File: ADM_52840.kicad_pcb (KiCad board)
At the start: 2 copper layers, 45 x 60 mm, 7 parts, among them U1 HolyIOT_NRF52840

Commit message: route & 3D
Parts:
- added C1: 100nF, LEGACY:SM0603, F.Cu at (118.6, 108.6)
- added C3: 1nF, LEGACY:SM0603, F.Cu at (103.7, 94.0)
- added C4: 10microF, LEGACY:SM0805, F.Cu at (131.9, 121.8)
- added C5: 10microF, LEGACY:SM0805, F.Cu at (115.6, 127.2)
- added C6: 10microF, LEGACY:SM0805, F.Cu at (116.7, 123.5)
- added D1: LED1, LEGACY:SM0603, F.Cu at (104.9, 99.0)
- added D2: LED2, LEGACY:SM0603, F.Cu at (107.8, 99.0)
- added D3: LED3, LEGACY:SM0603, F.Cu at (118.4, 118.5)
- added D4: MBR120, LEGACY:SOD-123, F.Cu at (125.4, 132.7)
- added D5: SK6812, LEGACY:WS2812B, F.Cu at (106.6, 111.8)
- added P1: USB_micro_B, LEGACY:USB_Micro-B, F.Cu at (132.0, 138.9)
- added Q1: DMP2045U, LEGACY:SOT23, F.Cu at (123.7, 129.3)
- added R1: 806K, LEGACY:SM0603, F.Cu at (106.3, 95.3)
- added R2: 2M, LEGACY:SM0603, F.Cu at (106.3, 92.2)
- added R3: 10K, LEGACY:SM0603, F.Cu at (131.9, 119.4)
- added R4: 1K, LEGACY:SM0603, F.Cu at (115.8, 119.0)
- added R5: 100K, LEGACY:SM0603, F.Cu at (119.1, 127.3)
- added R6: 100K, LEGACY:SM0603, F.Cu at (125.4, 137.7)
- added R7: 330, LEGACY:SM0603, F.Cu at (104.9, 102.3)
- added R8: 330, LEGACY:SM0603, F.Cu at (107.8, 102.3)
- added SW1: BTN1, LEGACY:SWITCH_CMS, F.Cu at (107.7, 123.7)
- added SW2: BTN2, LEGACY:SWITCH_CMS, F.Cu at (107.7, 130.9)
- added SW3: RESET, LEGACY:SWITCH_CMS, F.Cu at (107.7, 138.1)
- added U2: GD25Q16, LEGACY:SON80P400X300X60-10N, F.Cu at (121.0, 104.4)
- added U3: MCP73831, Package_TO_SOT_SMD:SOT-23-5, F.Cu at (123.4, 120.3)
- added U4: AP2127K-3.3, LEGACY:SOT23-5, F.Cu at (123.4, 124.9)
- C2: value C -> 10microF; footprint MWL:SM0805 -> LEGACY:SM0805
- J1: value (none) -> JST; footprint Connector_PinHeader_2.54mm:PinHeader_1x22_P2.54mm_Vertical -> Connector_JST:JST_PH_S2B-PH-SM4-TB_1x02-1MP_P2.00mm_Horizontal
- J2: value (none) -> SK6812_OUT; footprint Connector_PinHeader_2.54mm:PinHeader_1x18_P2.54mm_Vertical -> LEGACY:pin_array_3x1
- J3: value (none) -> Conn_01x15_Male; footprint Connector_PinHeader_2.54mm:PinHeader_1x10_P2.54mm_Vertical -> Connector_PinSocket_2.54mm:PinSocket_1x15_P2.54mm_Vertical
- J4: value (none) -> Conn_01x19_Male; footprint Connector_PinHeader_1.27mm:PinHeader_2x05_P1.27mm_Vertical_SMD -> Connector_PinSocket_2.54mm:PinSocket_1x18_P2.54mm_Vertical
- J5: value (none) -> JTAG; footprint Connector_PinHeader_2.54mm:PinHeader_1x06_P2.54mm_Vertical -> Connector_PinSocket_2.54mm:PinSocket_2x03_P2.54mm_Vertical
- U1: footprint MWL:HolyIOT-NRF52840-Module -> LEGACY:HolyIOT-NRF52840-Module
- moved J1 57.7 mm to (135.2, 128.5), turned to 90 degrees
- moved J4 56.4 mm to (98.3, 84.2)
- moved J2 41.5 mm to (98.3, 135.3), turned to 270 degrees
- moved J3 39.8 mm to (138.7, 84.2)
- moved J5 5.43 mm to (127.0, 112.9), turned to 270 degrees
- moved C2 3.51 mm to (112.7, 101.9)
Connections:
- J1 pad 2: Net-(J1-Pad2) -> VBAT
- J2 pad 1: Net-(J2-Pad1) -> V_NRF
- J2 pad 2: Net-(J2-Pad2) -> Net-(D5-Pad4)
- J2 pad 3: Net-(J2-Pad3) -> GND
- J4 pad 1: V_NRF -> Net-(J4-Pad1)
- J4 pad 2: SWDIO -> Net-(J4-Pad2)
- J4 pad 3: GND -> Net-(J4-Pad3)
- J4 pad 4: SWDCLK -> Net-(J4-Pad4)
- U1 pad 10: Net-(J1-Pad10) -> SK_SIGNAL
- U1 pad 11: Net-(J1-Pad11) -> P0.31
- U1 pad 12: Net-(J1-Pad12) -> Net-(SW1-Pad2)
- U1 pad 13: Net-(J1-Pad13) -> Net-(SW2-Pad2)
- U1 pad 14: Net-(J1-Pad14) -> Net-(J4-Pad7)
- U1 pad 15: Net-(J1-Pad15) -> Net-(J4-Pad8)
- U1 pad 16: Net-(J1-Pad16) -> Net-(J4-Pad9)
- U1 pad 17: Net-(J1-Pad17) -> Net-(J4-Pad10)
- U1 pad 18: Net-(J1-Pad18) -> Net-(J4-Pad11)
- U1 pad 19: Net-(J1-Pad19) -> Net-(J4-Pad12)
- U1 pad 2: Net-(J1-Pad2) -> Net-(J4-Pad1)
- U1 pad 20: Net-(J1-Pad20) -> Net-(J4-Pad13)
- U1 pad 21: Net-(J1-Pad21) -> Net-(J4-Pad14)
- U1 pad 22: Net-(J1-Pad22) -> Net-(J4-Pad15)
- U1 pad 23: Net-(J2-Pad9) -> Net-(J3-Pad9)
- U1 pad 24: Net-(J2-Pad8) -> Net-(J3-Pad10)
- U1 pad 25: Net-(J2-Pad7) -> QSPI_0
- U1 pad 26: Net-(J2-Pad6) -> QSPI_CS
- U1 pad 27: Net-(J2-Pad5) -> Net-(J3-Pad11)
- U1 pad 28: Net-(J2-Pad4) -> Net-(J3-Pad12)
- U1 pad 29: Net-(J2-Pad3) -> Net-(J3-Pad13)
- U1 pad 3: Net-(J1-Pad3) -> Net-(J4-Pad2)
- U1 pad 30: Net-(J2-Pad2) -> Net-(J3-Pad14)
- U1 pad 31: Net-(J2-Pad1) -> Net-(J3-Pad15)
- U1 pad 33: Net-(J2-Pad18) -> Net-(J3-Pad1)
- U1 pad 34: Net-(J2-Pad17) -> Net-(J3-Pad2)
- U1 pad 35: Net-(J2-Pad16) -> Net-(J3-Pad3)
- U1 pad 36: Net-(J2-Pad15) -> Net-(J3-Pad4)
- U1 pad 39: Net-(J2-Pad14) -> Net-(J3-Pad5)
- U1 pad 4: Net-(J1-Pad4) -> Net-(J4-Pad3)
- U1 pad 40: Net-(J2-Pad13) -> Net-(J3-Pad6)
- U1 pad 41: Net-(J2-Pad12) -> Net-(J3-Pad7)
- U1 pad 42: Net-(J2-Pad11) -> Net-(J3-Pad8)
- U1 pad 43: Net-(J2-Pad10) -> QSPI_2
- U1 pad 45: Net-(J3-Pad10) -> D-
- U1 pad 46: Net-(J3-Pad9) -> D+
- U1 pad 47: Net-(J3-Pad8) -> VBUS
- U1 pad 48: Net-(J3-Pad7) -> Net-(SW3-Pad1)
- U1 pad 49: Net-(J3-Pad6) -> QSPI_CLK
- U1 pad 5: Net-(J1-Pad5) -> Net-(J4-Pad4)
- U1 pad 50: Net-(J3-Pad5) -> QSPI_1
- U1 pad 51: Net-(J3-Pad4) -> QSPI_3
- U1 pad 52: Net-(J3-Pad3) -> Net-(J4-Pad18)
- U1 pad 53: Net-(J3-Pad2) -> Net-(J4-Pad17)
- U1 pad 54: Net-(J3-Pad1) -> Net-(J4-Pad16)
- U1 pad 6: Net-(J1-Pad6) -> Net-(J4-Pad5)
- U1 pad 7: Net-(J1-Pad7) -> Net-(J4-Pad6)
- U1 pad 8: Net-(J1-Pad8) -> Net-(D1-Pad2)
- U1 pad 9: Net-(J1-Pad9) -> Net-(D2-Pad2)
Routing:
- net Net-(J1-Pad22): track 54.5 -> 0.00 mm, vias 1 -> 0
- net Net-(J1-Pad21): track 53.5 -> 0.00 mm, vias 1 -> 0
- net Net-(J1-Pad20): track 51.9 -> 0.00 mm, vias 1 -> 0
- net Net-(J1-Pad19): track 50.5 -> 0.00 mm, vias 1 -> 0
- net Net-(J1-Pad18): track 50.1 -> 0.00 mm, vias 2 -> 0
- net D+: track 0.00 -> 49.9 mm, vias 0 -> 4
- net Net-(J1-Pad17): track 49.2 -> 0.00 mm, vias 2 -> 0
- net V_NRF: track 52.5 -> 3.47 mm, vias 2 -> 0
- net D-: track 0.00 -> 47.5 mm, vias 0 -> 4
- net Net-(J1-Pad16): track 47.1 -> 0.00 mm, vias 2 -> 0
- net Net-(J1-Pad14): track 46.4 -> 0.00 mm, vias 2 -> 0
- net Net-(J1-Pad15): track 46.3 -> 0.00 mm, vias 2 -> 0
- net Net-(SW3-Pad1): track 0.00 -> 46.0 mm, vias 0 -> 4
- net VBUS: track 0.00 -> 45.4 mm, vias 0 -> 3
- net Net-(J2-Pad3): track 44.2 -> 0.00 mm, vias 2 -> 0
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- added copper zone on F.Cu, net V_NRF
- removed copper zone on F.Cu, net GND
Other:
- board text removed: "D+"
- board text removed: "D-"
- board text removed: "GND"
- board text removed: "HolyIOT_NRF52840"
- board text removed: "P0.02"
- board text removed: "P0.03"
- board text removed: "P0.04"
- board text removed: "P0.05"
- board text removed: "P0.06"
- board text removed: "P0.07"
- board text removed: "P0.08"
- board text removed: "P0.09"
- board text removed: "P0.10"
- board text removed: "P0.11"
- board text removed: "P0.12"
- board text removed: "P0.13"
- board text removed: "P0.14"
- board text removed: "P0.15"
- board text removed: "P0.16"
- board text removed: "P0.17"
- board text removed: "P0.18/RST"
- board text removed: "P0.19"
- board text removed: "P0.20"
- board text removed: "P0.21"
- board text removed: "P0.22"
- board text removed: "P0.23"
- board text removed: "P0.24"
- board text removed: "P0.25"
- board text removed: "P0.26"
- board text removed: "P0.27"
- board text removed: "P0.28"
- board text removed: "P0.29"
- board text removed: "P0.30"
- board text removed: "P0.31"
- board text removed: "P1.00"
- board text removed: "P1.01"
- board text removed: "P1.02"
- board text removed: "P1.03"
- board text removed: "P1.04"
- board text removed: "P1.05"
- board text removed: "P1.06"
- board text removed: "P1.07"
- board text removed: "P1.08"
- board text removed: "P1.09"
- board text removed: "P1.10"
- board text removed: "P1.11"
- board text removed: "P1.12"
- board text removed: "P1.13"
- board text removed: "P1.14"
- board text removed: "P1.15"
- board text removed: "SWDCLK"
- board text removed: "SWDIO"
- board text removed: "V1.1"
- board text removed: "VBUS (5V)"
- board text removed: "VDD (3V)"
- board text removed: "www.anderson69s.com"

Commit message: 3D
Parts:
- U3: footprint Package_TO_SOT_SMD:SOT-23-5 -> LEGACY:SOT23-5
- moved J5 1.22 mm to (126.8, 114.1)
- turned R5 to 90 degrees
- turned U3 to 90 degrees
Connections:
- D2 pad 1: (no net) -> Net-(D2-Pad1)
- P1 pad 4: (no net) -> Net-(P1-Pad4)
- R8 pad 1: (no net) -> Net-(R8-Pad1)
- U4 pad 4: (no net) -> Net-(U4-Pad4)
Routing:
- net SWDCLK: track 31.3 -> 32.6 mm
- net SWDIO: track 35.9 -> 36.7 mm

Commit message: update alim
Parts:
- moved R3 14.4 mm to (117.8, 122.2), turned to 270 degrees
- moved R4 11.9 mm to (127.3, 121.9), turned to 90 degrees
- moved D3 9.70 mm to (128.1, 119.0)
- moved C5 7.00 mm to (118.5, 133.6), turned to 270 degrees
- moved C6 3.96 mm to (117.9, 127.3), turned to 90 degrees
- moved D4 3.67 mm to (122.2, 134.5), turned to 0 degrees
- moved R5 3.07 mm to (122.1, 128.1), turned to 0 degrees
- moved Q1 2.19 mm to (122.5, 131.1), turned to 90 degrees
- moved D5 2.08 mm to (106.6, 113.9)
- moved U3 1.95 mm to (122.0, 121.7)
- moved R6 1.66 mm to (123.8, 137.9)
- moved U4 1.47 mm to (122.1, 125.5), turned to 270 degrees
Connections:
- Q1 pad 1: Net-(C5-Pad1) -> VBUS
- Q1 pad 3: Net-(C5-Pad1) -> VBAT
- R8 pad 1: Net-(R8-Pad1) -> Net-(D2-Pad1)
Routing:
- net VBAT: track 11.3 -> 76.0 mm, vias 0 -> 9
- net VBUS: track 45.7 -> 68.6 mm, vias 3 -> 8
- net Net-(C5-Pad1): track 0.00 -> 15.4 mm
- net GND: track 39.2 -> 48.2 mm, vias 19 -> 21
- net Net-(R4-Pad1): track 0.00 -> 4.01 mm
- net Net-(R3-Pad2): track 5.61 -> 3.11 mm
- net Net-(D3-Pad1): track 0.00 -> 2.18 mm
- net SK_SIGNAL: track 19.3 -> 21.4 mm
- net Net-(R5-Pad1): track 0.00 -> 1.87 mm
- net Net-(D2-Pad1): track 0.00 -> 1.74 mm
- net (no net): track 1.74 -> 0.00 mm
- net Net-(D5-Pad4): track 25.2 -> 23.8 mm
- net Net-(J4-Pad16): track 33.9 -> 35.1 mm
- net Net-(J4-Pad18): track 38.4 -> 39.2 mm
- net Net-(J4-Pad17): track 36.3 -> 37.1 mm
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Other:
- net class Power added: clearance 0.4, trace_width 0.4, via_dia 0.8, via_drill 0.4
- rule via_min_size: 0.4 -> 0.3

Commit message: Seri + Corrections
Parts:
- J3: value Conn_01x15_Male -> Conn_01x16_Male; footprint Connector_PinSocket_2.54mm:PinSocket_1x15_P2.54mm_Vertical -> Connector_PinHeader_2.54mm:PinHeader_1x16_P2.54mm_Vertical
- J4: footprint Connector_PinSocket_2.54mm:PinSocket_1x18_P2.54mm_Vertical -> Connector_PinHeader_2.54mm:PinHeader_1x19_P2.54mm_Vertical
- J5: footprint Connector_PinSocket_2.54mm:PinSocket_2x03_P2.54mm_Vertical -> Connector_PinHeader_2.54mm:PinHeader_2x03_P2.54mm_Vertical
- moved C3 3.80 mm to (107.5, 93.6)
- moved J5 1.92 mm to (125.9, 112.4)
- moved J2 1.80 mm to (98.3, 137.1)
- moved R1 1.60 mm to (104.7, 95.6)
- moved R2 1.43 mm to (104.9, 92.0)
- moved J1 1.00 mm to (135.2, 129.5)
- moved R4 0.49 mm to (126.9, 121.9)
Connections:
- J5 pad 1: SWDIO -> SWDCLK
- J5 pad 2: SWDCLK -> SWDIO
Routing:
- net Net-(D5-Pad4): track 23.8 -> 25.7 mm
- net P0.31: track 10.6 -> 8.77 mm
- net VBUS: track 68.6 -> 67.2 mm
- net SWDIO: track 36.7 -> 37.9 mm
- net SWDCLK: track 32.6 -> 33.9 mm
- net VBAT: track 76.0 -> 74.8 mm
- net GND: track 48.2 -> 47.6 mm
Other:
- board text added: "3V"
- board text added: "ADM_B1_NRF52840"
- board text added: "GND"
- board text added: "JTAG"
- board text added: "P0.02"
- board text added: "P0.03"
- board text added: "P0.06"
- board text added: "P0.07"
- board text added: "P0.08"
- board text added: "P0.09"
- board text added: "P0.10"
- board text added: "P0.11"
- board text added: "P0.12"
- board text added: "P0.13"
- board text added: "P0.14"
- board text added: "P0.15"
- board text added: "P0.16"
- board text added: "P0.17"
- board text added: "P0.25"
- board text added: "P0.26"
- board text added: "P0.27"
- board text added: "P1.00"
- board text added: "P1.01"
- board text added: "P1.02"
- board text added: "P1.03"
- board text added: "P1.04"
- board text added: "P1.05"
- board text added: "P1.06"
- board text added: "P1.07"
- board text added: "P1.08"
- board text added: "P1.09"
- board text added: "P1.10"
- board text added: "P1.11"
- board text added: "P1.12"
- board text added: "P1.13"
- board text added: "P1.14"
- board text added: "P1.15"
- board text added: "SWDCLK"
- board text added: "SWDIO"
- board text added: "atelierdumaker.com"

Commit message: Logo
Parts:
- added G***: LOGO, LEGACY:adm_lite, F.Cu at (117.3, 136.2)
- added G***: LOGO, LEGACY:adm, B.Cu at (118.1, 128.7)
- moved C5 1.31 mm to (117.6, 132.6), turned to 180 degrees
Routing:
- net GND: track 47.6 -> 48.1 mm

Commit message: route
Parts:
- added C10: 100nF, LEGACY:SM0603, F.Cu at (114.4, 129.9)
- added C11: 100nF, LEGACY:SM0603, F.Cu at (104.1, 134.6)
- added C12: 10uF, LEGACY:SM0805, F.Cu at (128.2, 129.4)
- added C7: 10uF, LEGACY:SM0805, F.Cu at (117.7, 121.2)
- added C8: 100nF, LEGACY:SM0603, F.Cu at (113.6, 136.2)
- added C9: 100nF, LEGACY:SM0603, F.Cu at (104.5, 127.3)
- added R10: 10k mini, LEGACY:SM0603, F.Cu at (110.9, 126.9)
- added R11: 10k mini, LEGACY:SM0603, F.Cu at (113.6, 131.9)
- added R9: 10k mini, LEGACY:SM0603, F.Cu at (110.7, 134.4)
- J2: footprint LEGACY:pin_array_3x1 -> Connector_PinHeader_2.54mm:PinHeader_1x03_P2.54mm_Vertical
- moved J2 2.40 mm to (98.3, 134.7), turned to 0 degrees
- moved R3 1.40 mm to (117.6, 123.6), turned to 0 degrees
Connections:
- net Net-(SW1-Pad2) renamed P0.32
- net Net-(SW2-Pad2) renamed P0.33
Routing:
- net GND: track 48.1 -> 61.2 mm, vias 21 -> 22
- net P0.32: track 31.1 -> 40.0 mm, vias 0 -> 2
- net VBAT: track 74.8 -> 79.0 mm
- net P0.33: track 36.6 -> 39.9 mm
- net Net-(C8-Pad1): track 45.9 -> 48.6 mm
- net VBUS: track 67.2 -> 67.8 mm
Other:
- board text added: "-/S OUT/+"

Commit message: Done?
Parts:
- added ?: , , F.Cu at (130.8, 112.1)
- moved C7 13.4 mm to (130.5, 117.4), turned to 0 degrees
- moved Q1 13.1 mm to (124.3, 118.1), turned to 270 degrees
- moved R3 8.01 mm to (125.6, 123.2), turned to 90 degrees
- moved C5 7.75 mm to (119.9, 125.2)
- moved C9 7.64 mm to (110.0, 122.0), turned to 0 degrees
- moved U3 6.86 mm to (128.6, 123.7), turned to 0 degrees
- moved R10 6.43 mm to (106.7, 122.0), turned to 180 degrees
- moved C6 6.40 mm to (124.3, 127.2)
- moved D4 6.04 mm to (128.2, 134.5)
- moved D5 5.73 mm to (112.3, 114.7), turned to 0 degrees
- moved R9 5.66 mm to (113.7, 139.2), turned to 0 degrees
- moved U4 5.55 mm to (123.0, 131.0)
- moved R5 4.94 mm to (118.1, 131.1), turned to 90 degrees
- moved G*** 4.06 mm to (114.7, 126.5)
- moved R4 3.62 mm to (123.5, 123.2)
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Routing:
- net VBAT: track 79.0 -> 65.7 mm, vias 9 -> 4
- net Net-(D5-Pad4): track 25.7 -> 38.9 mm, vias 0 -> 6
- net Net-(C5-Pad1): track 15.4 -> 26.3 mm, vias 0 -> 6
- net Net-(J4-Pad18): track 39.0 -> 45.0 mm, vias 1 -> 3
- net VBUS: track 67.8 -> 62.3 mm, vias 8 -> 6
- net Net-(J4-Pad16): track 35.1 -> 40.3 mm, vias 1 -> 3
- net Net-(J4-Pad17): track 37.0 -> 42.0 mm, vias 1 -> 3
- net SK_SIGNAL: track 21.4 -> 25.6 mm, vias 2 -> 4
- net Net-(D3-Pad1): track 2.34 -> 6.12 mm
- net GND: track 61.2 -> 58.7 mm, vias 22 -> 27
- net Net-(J4-Pad15): track 35.2 -> 32.8 mm
- net Net-(J4-Pad14): track 34.5 -> 32.2 mm
- net SWDCLK: track 33.9 -> 31.7 mm
- net V_NRF: track 3.47 -> 5.37 mm
- net Net-(R5-Pad1): track 1.87 -> 3.64 mm
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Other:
- board text added: "3V/GND/SWDCLK"
- board text added: "3V/GND/SWDIO"
- board text added: "GND/OUT/3V"
- board text removed: "-/S OUT/+"
- board text removed: "JTAG"
- board text removed: "SWDCLK"
- board text removed: "SWDIO"

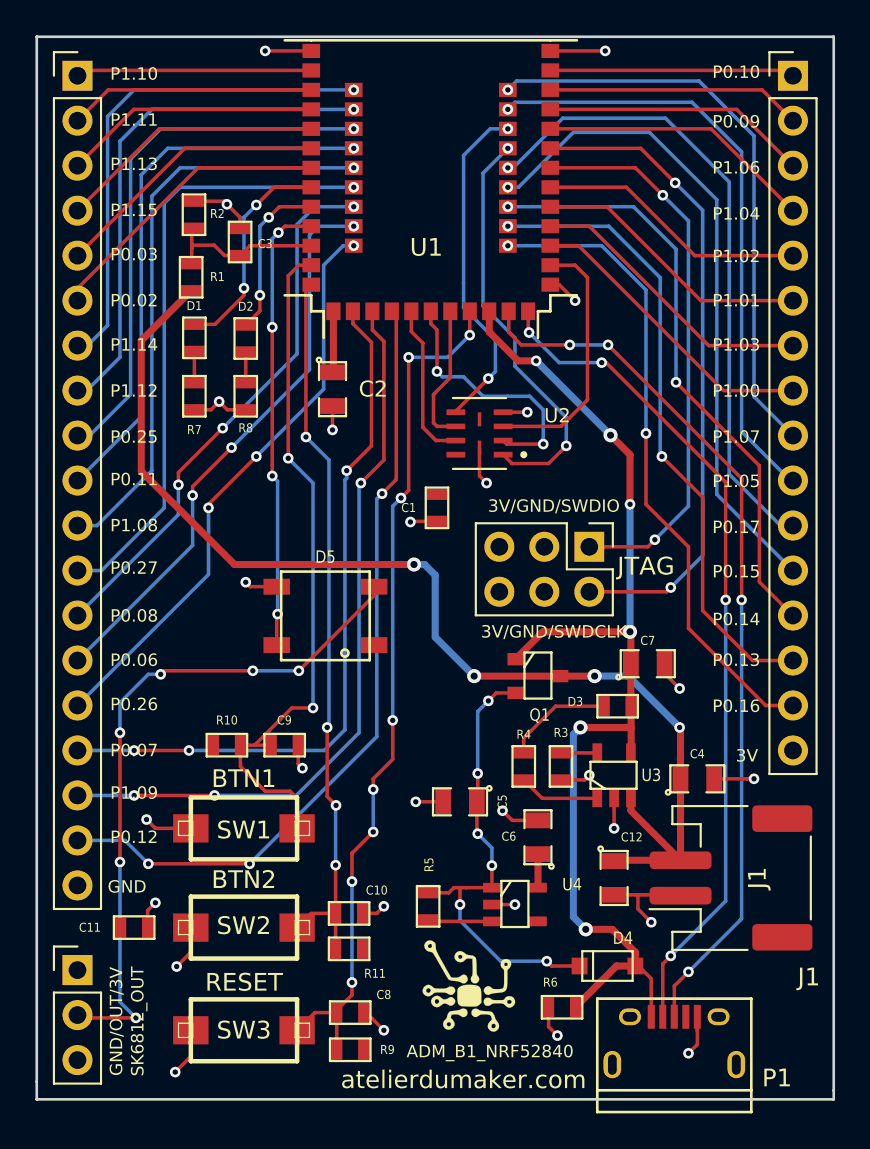
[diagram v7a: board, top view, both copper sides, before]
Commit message: Pinout SPi
Rework pinout SPI + SK6812 + Footprint SPI
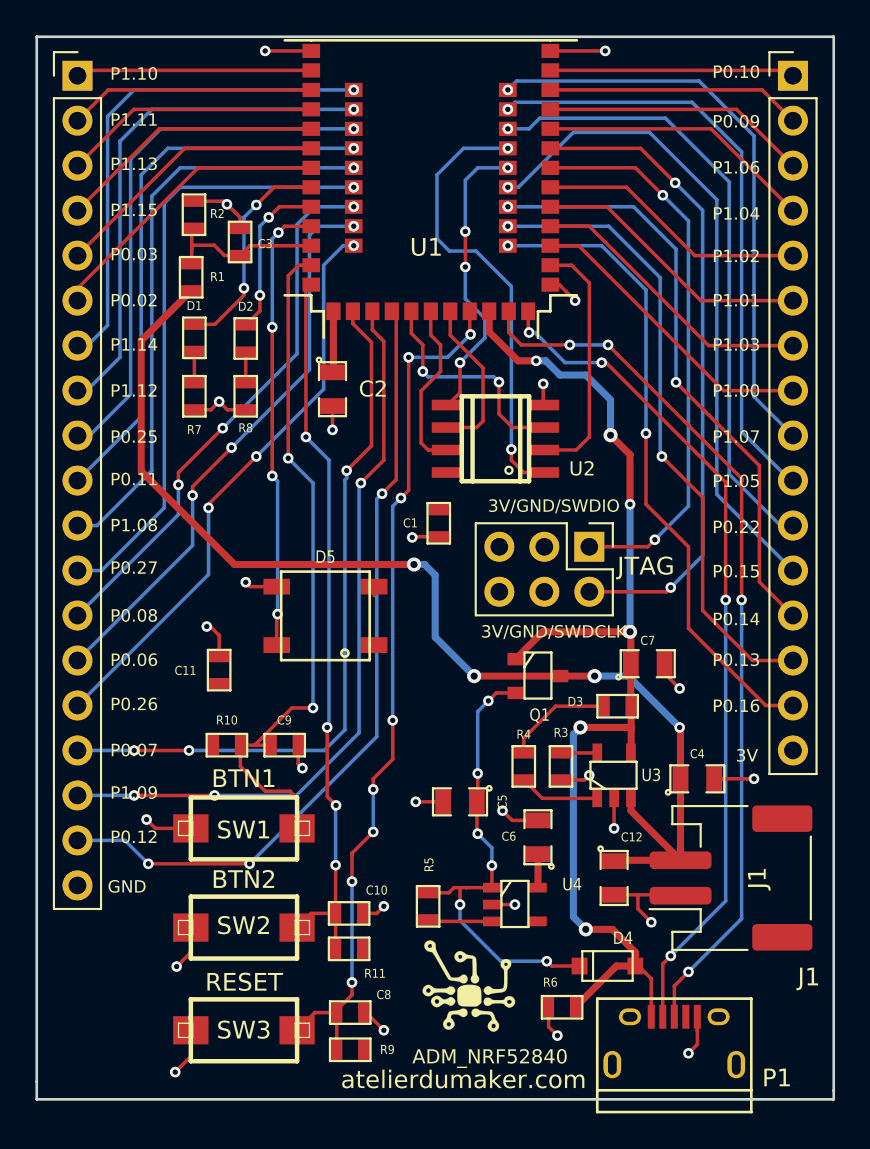
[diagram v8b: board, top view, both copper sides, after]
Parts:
- removed J2: SK6812_OUT, Connector_PinHeader_2.54mm:PinHeader_1x03_P2.54mm_Vertical
- U2: footprint LEGACY:SON80P400X300X60-10N -> LEGACY:SOIC8
- moved C11 15.3 mm to (106.3, 117.8), turned to 270 degrees
- moved U2 0.95 mm to (121.9, 104.7), turned to 90 degrees
- moved C1 0.88 mm to (118.7, 109.5)
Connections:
- net P0.32 renamed P0.04
- net P0.33 renamed P0.05
- U1 pad 25: QSPI_0 -> Net-(J3-Pad11)
- U1 pad 27: Net-(J3-Pad11) -> QSPI_0
- U1 pad 43: QSPI_2 -> QSPI_1
- U1 pad 50: QSPI_1 -> QSPI_3
- U1 pad 51: QSPI_3 -> QSPI_2
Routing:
- net Net-(D5-Pad4): track 38.9 -> 0.50 mm, vias 6 -> 0
- net QSPI_0: track 19.3 -> 16.7 mm, vias 2 -> 4
- net QSPI_CS: track 23.5 -> 25.4 mm
- net QSPI_2: track 14.7 -> 12.8 mm, vias 0 -> 2
- net GND: track 58.7 -> 56.8 mm, vias 27 -> 26
- net VBUS: track 62.3 -> 63.5 mm
- net QSPI_CLK: track 8.04 -> 9.11 mm
- net Net-(J3-Pad11): track 36.5 -> 35.5 mm
- net QSPI_3: track 9.00 -> 9.78 mm
- net QSPI_1: track 14.7 -> 14.2 mm, vias 2 -> 0
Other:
- board text added: "ADM_NRF52840"
- board text added: "P0.22"
- board text removed: "ADM_B1_NRF52840"
- board text removed: "GND/OUT/3V"
- board text removed: "P0.17"
